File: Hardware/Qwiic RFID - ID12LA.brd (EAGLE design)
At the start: 35.6 x 30.5 mm, 30 parts, among them J2 SMD, J3 PTH, J4 SMD, J8 AVR_SPI_PROG_3X2TESTPOINTS, U1 ATTINY84

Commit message: Schematic organization
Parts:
- removed J7: (no value), SparkFun-Connectors:1X01_NO_SILK
- moved J6 28.4 mm to (26.7, 1.27)
- moved J1 28.4 mm to (24.1, 1.27)
- moved R1 14.2 mm to (29.2, 24.1)
- moved J3 2.54 mm to (11.4, 1.27)
- moved J5 2.54 mm to (21.6, 1.27)
- moved D2 1.27 mm to (31.8, 2.54)
- moved R6 1.27 mm to (31.8, 3.81)
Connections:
- net CP: now also U1.6; no longer J7.1
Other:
- board text added: "Elias Santistevan"
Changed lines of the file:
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@@
 <layer number="45" name="Holes" color="7" fill="1" visible="yes" active="yes"/>
 <layer number="46" name="Milling" color="3" fill="1" visible="no" active="yes"/>
-<layer number="47" name="Measures" color="7" fill="1" visible="yes" active="yes"/>
+<layer number="47" name="Measures" color="7" fill="1" visible="no" active="yes"/>
 <layer number="48" name="Document" color="7" fill="1" visible="no" active="yes"/>
 <layer number="49" name="Reference" color="13" fill="1" visible="yes" active="yes"/>
@@
 <dimension x1="1.27" y1="30.48" x2="1.27" y2="0" x3="-7.62" y3="15.24" textsize="1.778" textratio="15" layer="47" unit="inch"/>
 <text x="0" y="41.91" size="1.778" layer="47" font="vector" ratio="15">Units in Inches</text>
+<text x="21.59" y="-10.16" size="1.778" layer="51" font="vector" ratio="15">Elias Santistevan</text>
 </plain>
 <attributes>
@@
 <element name="I2C" library="SparkFun-Jumpers" package="SMT-JUMPER_3_2-NC_TRACE_SILK" value="" x="19.05" y="5.08" rot="MR0"/>
 <element name="J2" library="SparkX" package="1X04_1MM_RA" value="SMD" x="6.35" y="15.24" rot="R270"/>
-<element name="J3" library="SparkX" package="1X04_NO_SILK" value="PTH" x="13.97" y="1.27"/>
+<element name="J3" library="SparkX" package="1X04_NO_SILK" value="PTH" x="11.43" y="1.27"/>
 <element name="FRAME1" library="SparkFun-Aesthetics" package="CREATIVE_COMMONS" value="FRAME-LETTER" x="-8.89" y="-10.16"/>
 <element name="J4" library="SparkX" package="1X04_1MM_RA" value="SMD" x="31.75" y="15.24" rot="R90"/>
 <element name="LOGO1" library="SparkFun-Aesthetics" package="OSHW-LOGO-MINI" value="OSHW-LOGOMINI" x="3.81" y="3.81" rot="MR0"/>
-<element name="J5" library="SparkFun-Connectors" package="1X01_NO_SILK" value="" x="24.13" y="1.27"/>
-<element name="R1" library="SparkFun-Resistors" package="0603" value="10k" x="15.24" y="21.59" rot="R90">
-<attribute name="PROD_ID" value="RES-00824" x="15.24" y="21.59" size="1.778" layer="27" font="vector" ratio="15" rot="R90" display="off"/>
+<element name="J5" library="SparkFun-Connectors" package="1X01_NO_SILK" value="" x="21.59" y="1.27"/>
+<element name="R1" library="SparkFun-Resistors" package="0603" value="10k" x="29.21" y="24.13" rot="R90">
+<attribute name="PROD_ID" value="RES-00824" x="29.21" y="24.13" size="1.778" layer="27" font="vector" ratio="15" rot="R90" display="off"/>
 </element>
 <element name="JP1" library="SparkFun" package="MICRO-FIDUCIAL" value="FIDUCIALUFIDUCIAL" x="2.032" y="29.718" rot="MR0"/>
@@
 <attribute name="PROD_ID" value="CONN-09345, CONN-09344" x="18.923" y="15.24" size="1.778" layer="27" font="vector" ratio="15" rot="R90" display="off"/>
 </element>
-<element name="J1" library="SparkFun-Connectors" package="1X01_NO_SILK" value="" x="19.05" y="29.21" rot="R90"/>
-<element name="J6" library="SparkFun-Connectors" package="1X01_NO_SILK" value="" x="21.59" y="29.21" rot="R90"/>
-<element name="J7" library="SparkFun-Connectors" package="1X01_NO_SILK" value="" x="16.51" y="29.21" rot="R90"/>
+<element name="J1" library="SparkFun-Connectors" package="1X01_NO_SILK" value="" x="24.13" y="1.27" rot="R90"/>
+<element name="J6" library="SparkFun-Connectors" package="1X01_NO_SILK" value="" x="26.67" y="1.27" rot="R90"/>
 <element name="J8" library="SparkFun-Connectors" package="2X3_TEST_POINTS" value="AVR_SPI_PROG_3X2TESTPOINTS" x="19.05" y="22.86" rot="MR0"/>
 <element name="R2" library="SparkFun-Resistors" package="0603" value="4.7k" x="13.97" y="6.35">
 <attribute name="PROD_ID" value="RES-07857" x="13.97" y="6.35" size="1.778" layer="27" font="vector" ratio="15" display="off"/>
 </element>
-<element name="D2" library="SparkFun-LED" package="LED-0603" value="BLUE" x="30.48" y="2.54">
-<attribute name="PROD_ID" value="DIO-08575" x="30.48" y="2.54" size="1.778" layer="27" font="vector" ratio="15" display="off"/>
-</element>
-<element name="R6" library="SparkFun-Resistors" package="0603" value="1k" x="30.48" y="3.81" rot="R180">
-<attribute name="PROD_ID" value="RES-07856" x="30.48" y="3.81" size="1.778" layer="27" font="vector" ratio="15" rot="R180" display="off"/>
+<element name="D2" library="SparkFun-LED" package="LED-0603" value="BLUE" x="31.75" y="2.54">
+<attribute name="PROD_ID" value="DIO-08575" x="31.75" y="2.54" size="1.778" layer="27" font="vector" ratio="15" display="off"/>
+</element>
+<element name="R6" library="SparkFun-Resistors" package="0603" value="1k" x="31.75" y="3.81" rot="R180">
+<attribute name="PROD_ID" value="RES-07856" x="31.75" y="3.81" size="1.778" layer="27" font="vector" ratio="15" rot="R180" display="off"/>
 </element>
 </elements>
@@
 <wire x1="24.9212" y1="16.2334" x2="31.75" y2="14.74" width="0" layer="19" extent="1-1"/>
 <wire x1="21.59" y1="24.13" x2="24.9212" y2="16.2334" width="0" layer="19" extent="1-1"/>
-<wire x1="15.24" y1="22.44" x2="21.59" y2="24.13" width="0" layer="19" extent="1-1"/>
-<wire x1="12.9098" y1="22.2334" x2="15.24" y2="22.44" width="0" layer="19" extent="1-1"/>
-<wire x1="16.25" y1="18.415" x2="15.24" y2="22.44" width="0" layer="19" extent="1-1"/>
+<wire x1="29.21" y1="24.98" x2="21.59" y2="24.13" width="0" layer="19" extent="1-1"/>
+<wire x1="12.9098" y1="22.2334" x2="29.21" y2="24.98" width="0" layer="19" extent="1-1"/>
+<wire x1="16.25" y1="18.415" x2="29.21" y2="24.98" width="0" layer="19" extent="1-1"/>
 <wire x1="6.35" y1="15.74" x2="12.9098" y2="22.2334" width="0" layer="19" extent="1-1"/>
 <wire x1="14.82" y1="6.35" x2="6.35" y2="15.74" width="0" layer="19" extent="1-1"/>
 <wire x1="19.05" y1="5.08" x2="14.82" y2="6.35" width="0" layer="19" extent="1-16"/>
-<wire x1="16.51" y1="1.27" x2="19.05" y2="5.08" width="0" layer="19" extent="16-16"/>
+<wire x1="13.97" y1="1.27" x2="19.05" y2="5.08" width="0" layer="19" extent="16-16"/>
 <wire x1="4.66" y1="8.89" x2="14.82" y2="6.35" width="0" layer="19" extent="1-1"/>
 </signal>
@@
 <contactref element="J3" pad="1"/>
 <contactref element="J4" pad="1"/>
-<contactref element="JP7" pad="1"/>
 <contactref element="U1" pad="14"/>
 <contactref element="J8" pad="6"/>
@@
 <contactref element="D2" pad="C"/>
 <contactref element="D1" pad="C"/>
+<contactref element="JP7" pad="1"/>
 <wire x1="27.9212" y1="18.2334" x2="31.75" y2="13.74" width="0" layer="19" extent="1-1"/>
 <wire x1="21.85" y1="18.415" x2="27.9212" y2="18.2334" width="0" layer="19" extent="1-1"/>
 <wire x1="16.51" y1="24.13" x2="21.85" y2="18.415" width="0" layer="19" extent="1-1"/>
-<wire x1="31.357" y1="2.54" x2="31.75" y2="13.74" width="0" layer="19" extent="1-1"/>
+<wire x1="32.627" y1="2.54" x2="31.75" y2="13.74" width="0" layer="19" extent="1-1"/>
 <wire x1="6.35" y1="16.74" x2="16.51" y2="24.13" width="0" layer="19" extent="1-1"/>
 <wire x1="9.9098" y1="12.2334" x2="6.35" y2="16.74" width="0" layer="19" extent="1-1"/>
+<wire x1="4.687" y1="10.16" x2="9.9098" y2="12.2334" width="0" layer="19" extent="1-1"/>
 <wire x1="3.4036" y1="22.86" x2="6.35" y2="16.74" width="0" layer="19" extent="1-1"/>
-<wire x1="4.687" y1="10.16" x2="9.9098" y2="12.2334" width="0" layer="19" extent="1-1"/>
-<wire x1="13.97" y1="1.27" x2="4.687" y2="10.16" width="0" layer="19" extent="1-1"/>
+<wire x1="11.43" y1="1.27" x2="9.9098" y2="12.2334" width="0" layer="19" extent="1-1"/>
 </signal>
 <signal name="SCL">
@@
 <contactref element="J3" pad="4"/>
 <contactref element="J4" pad="4"/>
-<wire x1="21.59" y1="1.27" x2="31.75" y2="16.74" width="0" layer="19" extent="1-1"/>
-<wire x1="6.35" y1="13.74" x2="21.59" y2="1.27" width="0" layer="19" extent="1-1"/>
+<wire x1="19.05" y1="1.27" x2="31.75" y2="16.74" width="0" layer="19" extent="1-1"/>
+<wire x1="6.35" y1="13.74" x2="19.05" y2="1.27" width="0" layer="19" extent="1-1"/>
 </signal>
 <signal name="SDA">
@@
 <contactref element="J3" pad="3"/>
 <contactref element="J4" pad="3"/>
-<wire x1="19.05" y1="1.27" x2="31.75" y2="15.74" width="0" layer="19" extent="1-1"/>
-<wire x1="6.35" y1="14.74" x2="19.05" y2="1.27" width="0" layer="19" extent="1-1"/>
+<wire x1="16.51" y1="1.27" x2="31.75" y2="15.74" width="0" layer="19" extent="1-1"/>
+<wire x1="6.35" y1="14.74" x2="16.51" y2="1.27" width="0" layer="19" extent="1-1"/>
 </signal>
 <signal name="!INT">
@@
 <contactref element="U$3" pad="3"/>
 <contactref element="J1" pad="1"/>
-<wire x1="27.9212" y1="14.2334" x2="19.05" y2="29.21" width="0" layer="19" extent="1-1"/>
+<wire x1="27.9212" y1="14.2334" x2="24.13" y2="1.27" width="0" layer="19" extent="1-1"/>
 </signal>
 <signal name="ANT2">
 <contactref element="U$3" pad="4"/>
 <contactref element="J6" pad="1"/>
-<wire x1="24.9212" y1="12.2334" x2="21.59" y2="29.21" width="0" layer="19" extent="1-1"/>
+<wire x1="24.9212" y1="12.2334" x2="26.67" y2="1.27" width="0" layer="19" extent="1-1"/>
 </signal>
 <signal name="CP">
 <contactref element="U$3" pad="5"/>
-<contactref element="J7" pad="1"/>
-<wire x1="27.9212" y1="10.2334" x2="16.51" y2="29.21" width="0" layer="19" extent="1-1"/>
+<contactref element="U1" pad="6"/>
+<wire x1="16.25" y1="12.065" x2="27.9212" y2="10.2334" width="0" layer="19" extent="1-1"/>
 </signal>
 <signal name="MISO">
@@
 <contactref element="D2" pad="A"/>
 <contactref element="R6" pad="1"/>
-<wire x1="29.603" y1="2.54" x2="31.33" y2="3.81" width="0" layer="19" extent="1-1"/>
+<wire x1="30.873" y1="2.54" x2="32.6" y2="3.81" width="0" layer="19" extent="1-1"/>
 </signal>
 <signal name="RFID_LED">
 <contactref element="R6" pad="2"/>
 <contactref element="U$3" pad="10"/>
-<wire x1="12.9098" y1="18.2334" x2="29.63" y2="3.81" width="0" layer="19" extent="1-1"/>
+<wire x1="12.9098" y1="18.2334" x2="30.9" y2="3.81" width="0" layer="19" extent="1-1"/>
 </signal>
 <signal name="N$2">
@@
 <contactref element="JP8" pad="2"/>
 <contactref element="R1" pad="1"/>
-<wire x1="15.24" y1="20.74" x2="31.75" y2="23.622" width="0" layer="19" extent="1-16"/>
+<wire x1="29.21" y1="23.28" x2="31.75" y2="23.622" width="0" layer="19" extent="1-16"/>
 </signal>
 <signal name="DO">

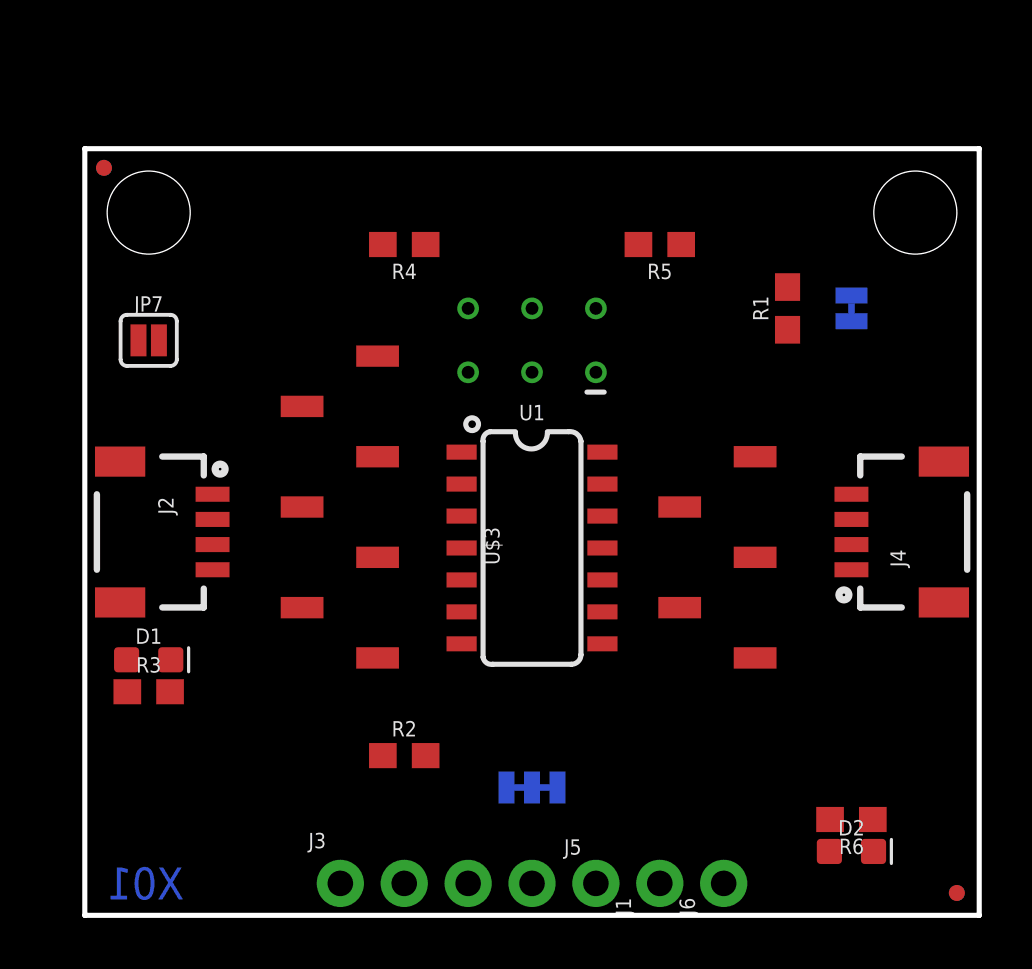
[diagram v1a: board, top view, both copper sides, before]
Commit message: Moved to double sided to decrease size of product
Buzzer, LED, and RFID connector live on top.
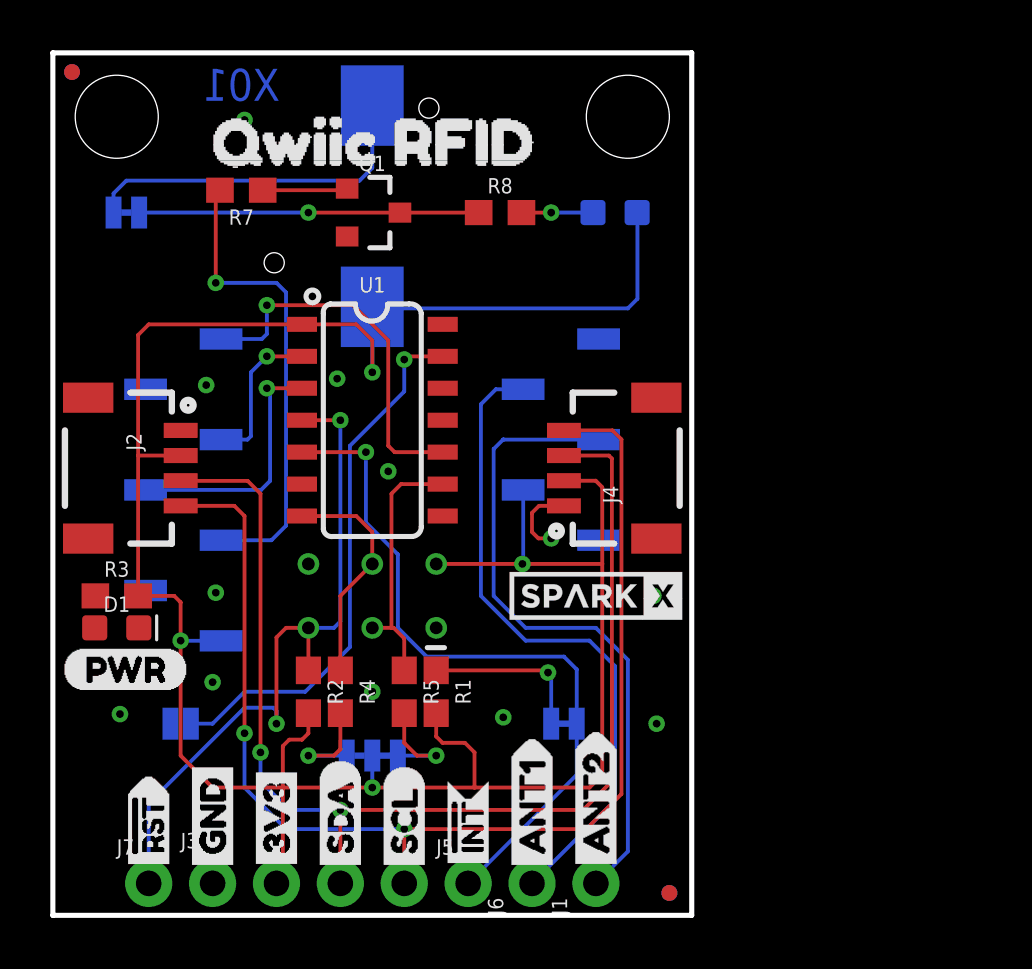
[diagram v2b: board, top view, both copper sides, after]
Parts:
- removed R6: 1k, SparkFun-Resistors:0603
- removed U$3: ID-12/20SMD, SparkFun-RF:ID-12_SMD
- added J7: (no value), SparkFun-Connectors:1X01_NO_SILK
- added JP9: BUZZ, SparkFun-Jumpers:SMT-JUMPER_2_NC_TRACE_SILK
- added LS1: BUZZER-SMD, SparkFun-Electromechanical:BUZZER-CCV
- added Q1: 600mA/40V, SparkFun-DiscreteSemi:SOT23-3
- added R7, R8: 1k, SparkFun-Resistors:0603
- added U$1: (no value), Labels:PWR-()-04
- added U$10: (no value), Labels:3V3-04
- added U$11: (no value), Labels:INT#-[<
- added U$12: (no value), Labels:I2C-()
- added U$13: (no value), Labels:INT-()
- added U$14: (no value), Labels:ADR-()
- added U$15: (no value), BUZZER:BUZZER0
- added U$16: (no value), ANT1:ANT10
- added U$17: (no value), ANT2:ANT20
- added U$18: (no value), READ:READ0
- added U$19: (no value), QWIIC_RFID:QWIIC_RFID0
- added U$2: (no value), SparkX:SPARKX-SMALL
- added U$4: SPARKX-LOGO3, SparkX:SPARKX-SMALL
- added U$5: (no value), Labels:RST#-[>
- added U$6: (no value), Labels:SDA-[)
- added U$7: (no value), Labels:SCL-[)
- added U$9: (no value), Labels:GND-04
- added U2: ID-12/20SMD, SparkFun-RF:ID-12_SMD
- R2: value 4.7k -> 10k
- moved D2 27.1 mm to (22.4, 27.9), flipped to the bottom
- moved U$8 24.0 mm to (12.7, 17.8)
- moved LOGO1 20.9 mm to (23.7, 10.2)
- moved R1 20.7 mm to (15.2, 8.89), turned to 270 degrees
- moved R5 20.5 mm to (14.0, 8.89), turned to 270 degrees
- moved JP8 20.1 mm to (20.3, 7.62), turned to 0 degrees
- moved R4 18.0 mm to (11.4, 8.89), turned to 270 degrees
- moved JP7 15.3 mm to (5.08, 7.62), flipped to the bottom, turned to 180 degrees
- moved JP4 12.0 mm to (22.9, 31.8)
- moved J8 12.0 mm to (12.7, 12.7)
- moved J4 11.7 mm to (20.3, 17.8)
- moved JP2 11.4 mm to (24.5, 0.89)
- moved JP5 11.4 mm to (24.5, 0.89)
- moved U1 8.13 mm to (12.7, 20.3)
- moved J6 7.62 mm to (19.1, 1.27)
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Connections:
- removed net CP: U$3.5, U1.6
- removed net D0: U$3.9
- removed net N$11: D2.A, R6.1
- removed net RFID_LED: R6.2, U$3.10
- new net LED_BUZZ: R7.2, U2.10
- new net N$5: D2.C, R8.2
- new net N$8: JP9.1, Q1.3, R8.1
- new net N$9: JP9.2, LS1.-
- net !INT: now also JP8.1, U1.5
- net !RST: now also J7.1
- net 3.3V: now also D2.A, LS1.+, U2.11, U2.2; no longer U$3.11, U$3.2
- net ANT1: now also U2.3; no longer U$3.3
- net ANT2: now also U2.4; no longer U$3.4
- net D1: now also U2.8; no longer U$3.8
- net DO: now also U2.9
- net GND: now also Q1.2, U2.1, U2.7; no longer D2.C, U$3.1, U$3.7
- net N$7: now also Q1.1, R7.1; no longer JP8.1, U1.5
- net TAG_IN_RANGE: now also U2.6; no longer U$3.6
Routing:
- net 3.3V: track 0.00 -> 102.5 mm, vias 0 -> 4
- net SCL: track 0.00 -> 49.1 mm, vias 0 -> 2
- net SDA: track 0.00 -> 47.9 mm, vias 0 -> 2
- net !INT: track 0.00 -> 28.2 mm, vias 0 -> 1
- net !RST: track 0.00 -> 27.8 mm, vias 0 -> 2
- net ANT2: track 0.00 -> 26.0 mm
- net ANT1: track 0.00 -> 26.0 mm
- net N$6: track 0.00 -> 21.5 mm, vias 0 -> 1
- net LED_BUZZ: track 0.00 -> 18.8 mm, vias 0 -> 1
- net TAG_IN_RANGE: track 0.00 -> 14.9 mm, vias 0 -> 1
- net N$9: track 0.00 -> 13.9 mm
- net N$8: track 0.00 -> 13.5 mm, vias 0 -> 1
- net SCL/SCK: track 0.00 -> 10.2 mm
- net DO: track 0.00 -> 10.2 mm, vias 0 -> 1
- net SDA/MOSI: track 0.00 -> 9.09 mm
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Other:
- board size 35.6 x 30.5 mm -> 25.4 x 34.3 mm
